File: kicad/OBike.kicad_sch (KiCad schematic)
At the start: 74 parts, among them J1 F34G-1A7Q1-E8C40, J2 Micro_SD_Card_Det1, J3 Conn_01x02, J4 Conn_01x04, J5 U.FL-R-SMT-1_10_, J6 Conn_01x02, J7 Conn_01x05, J8 Conn_01x02, Q1 SS8050, Q2 SS8050, SW1 5_position_tactile, U1 DPS368XTSA1, U10 MAX40200AUK, U2 DS3231M, U3 MCP23017_SO, U4 74HC14, U5 Seeed Studio XIAO SAMD21, U6 MAX40200AUK, U7 LC76G, U8 MAX40200AUK, U9 W25N01GVZEIG_TR

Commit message: purchased PCBs
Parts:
- removed R13: 0R, Resistor_SMD:R_0603_1608Metric, symbol Device:R
- removed U2: DS3231M, Package_SO:SOIC-8_3.9x4.9mm_P1.27mm, symbol Timer_RTC:DS3231M
- added U2: PCF8523T, Package_SO:SOIC-8_3.9x4.9mm_P1.27mm, symbol Timer_RTC:PCF8523T
- C1, C10, C11, C12, C13, C14, C18, C19, C3, C4, C5, C6, C7, C8, C9: MANUFACTURER (none) -> Samsung
- C16, C17, C20, C21: MANUFACTURER (none) -> KEMET
- C2: Digikey PN (none) -> 1276-1066-1-ND; MANUFACTURER 1276-1066-1-ND -> Samsung
- D1, D2, D3, D4, D5: MANUFACTURER (none) -> SMC Diode Solutions
- D6, D7: MANUFACTURER (none) -> STMicroelectronics
- J2: MANUFACTURER (none) -> Same Sky
- J3: MANUFACTURER (none) -> JST
- LS1: value ASI09N40MTRQ -> BUZZER MAGNETIC 5V8.5X8.5 SMD; footprint Mallory:ASI09N40M -> CUI:CUI_CMT-8540S-SMT; Digikey PN 458-ASI09N40MTRQCT-ND -> 102-3746-1-ND; MANUFACTURER (none) -> Same Sky (Formerly CUI Devices)
- Q1, Q2: MANUFACTURER (none) -> MCC
- R36: Digikey PN RMCF0805JT10K0CT-ND -> RMCF0603JT47R0CT-ND
- SW1: MANUFACTURER (none) -> TE Connectivity
- U1: MANUFACTURER (none) -> Infineon Technologies
- U10, U6, U8: MANUFACTURER (none) -> Analog Devices Inc
- U3: MANUFACTURER (none) -> Microchip
- U4: MANUFACTURER (none) -> Toshiba Semiconductor
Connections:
- net 3V3: now also U2.8 (VDD)
- net GND: now also U2.4 (VSS)
- net SCL: now also U2.6 (SCL)
- net SDA: now also U2.5 (SDA)

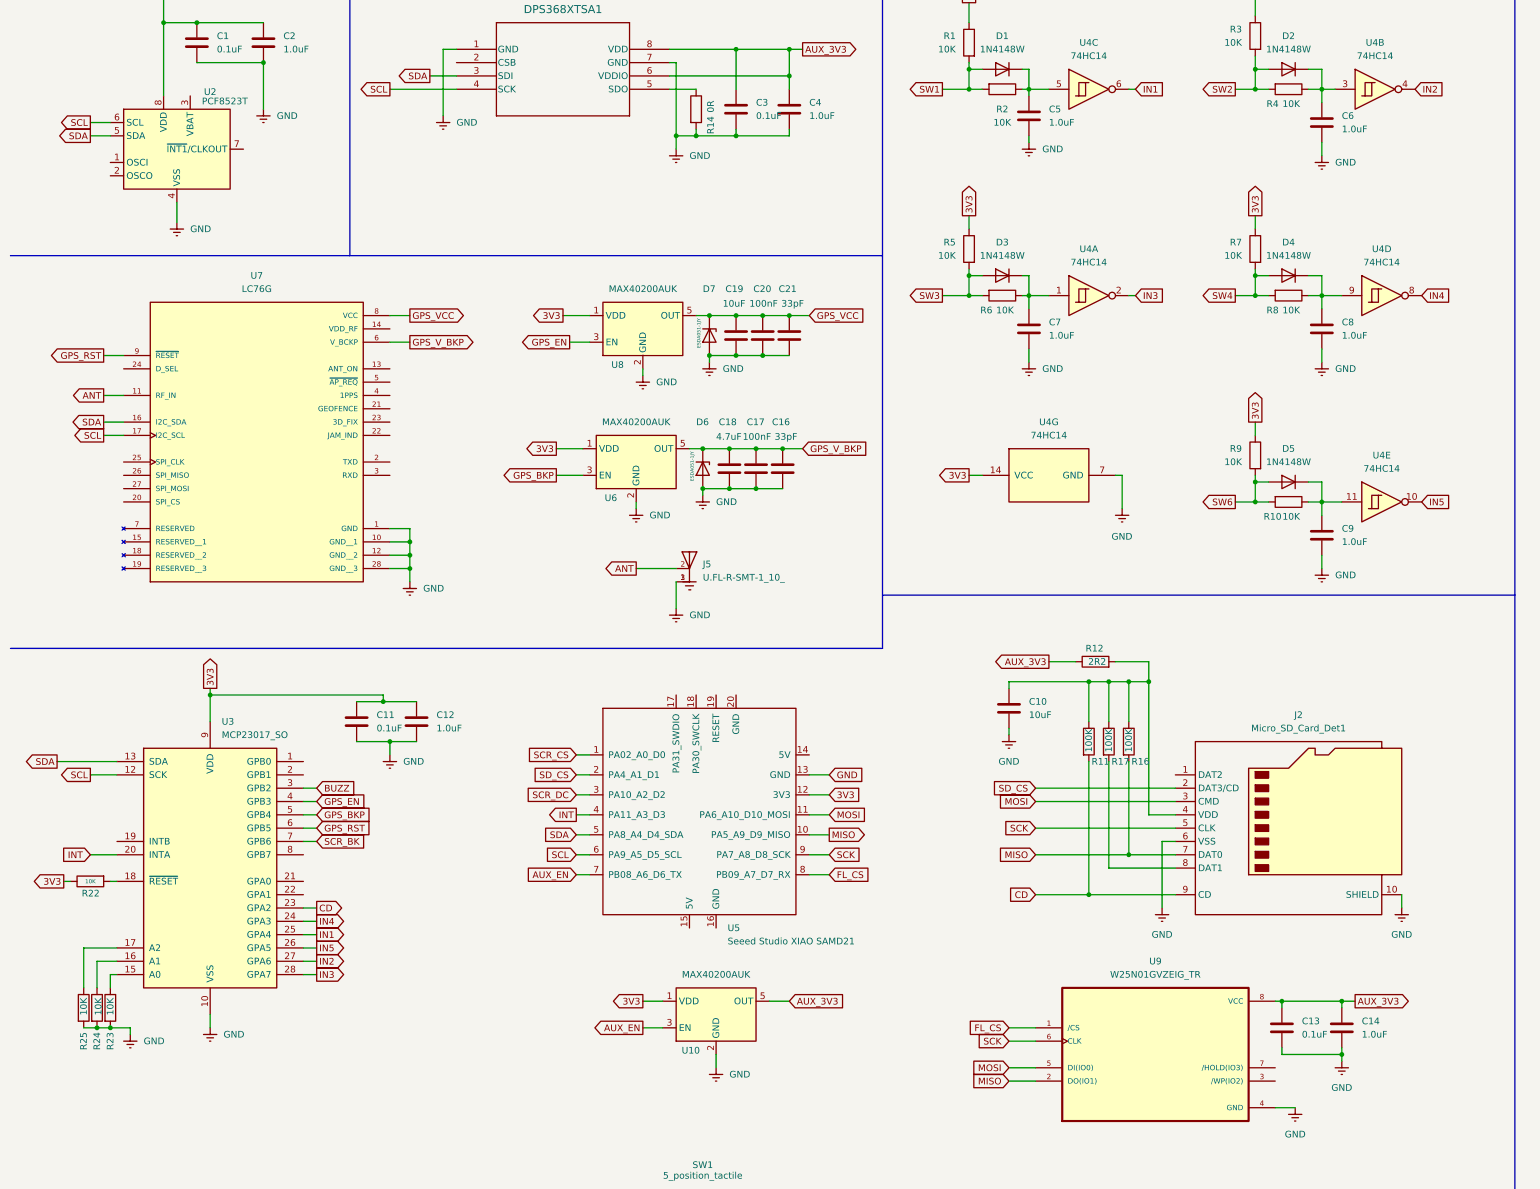
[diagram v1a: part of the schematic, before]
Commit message: pcb fixes
- WP and Hold pins on flash shorted to aux 3v3
- added a 32.768khz crystal for the RTC
- fixed wrong part numbers for Q1 & Q2
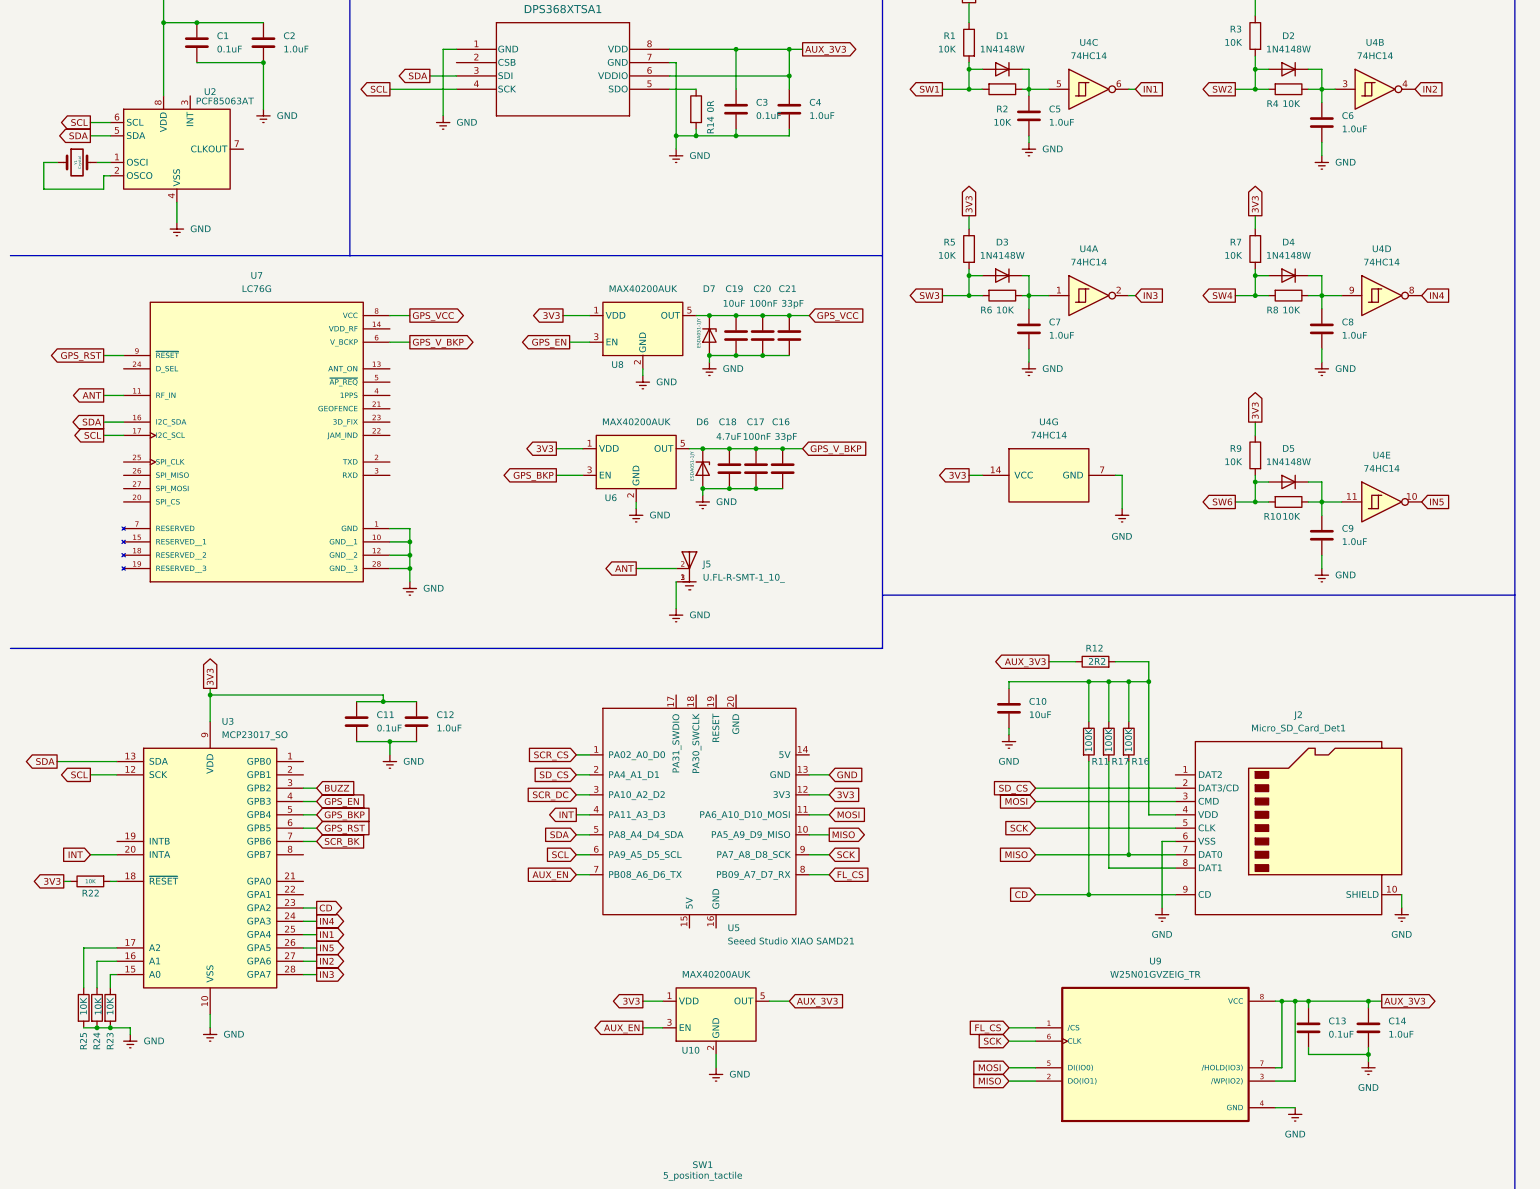
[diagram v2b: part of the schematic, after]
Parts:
- added Y1: Crystal, Jauch:OSCSC320X150X90, symbol Device:Crystal
- Q1, Q2: Digikey PN MMSS8550-H-TPMSCT-ND -> MMSS8050-H-TPMSCT-ND
- U2: value PCF8523T -> PCF85063AT
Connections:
- net AUX_3V3: now also U9.3 (/WP(IO2)), U9.7 (/HOLD(IO3))
- net at U2.1 (OSCI): now also Y1.2
- net at U2.2 (OSCO): now also Y1.1
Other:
- moved on the sheet: C13, C14

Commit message: ui updates
- also disp reset working
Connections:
- net SCR_RST: now reaches J1.15
- net SCR_RST: now also U3.8 (GPB7)
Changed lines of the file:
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@@
 	(wire
 		(pts
+			(xy 364.49 59.69) (xy 382.27 59.69)
+		)
+		(stroke
+			(width 0)
+			(type default)
+		)
+	)
+	(wire
+		(pts
 			(xy 396.24 233.68) (xy 396.24 240.03)
 		)
@@
 	(wire
 		(pts
+			(xy 68.58 185.42) (xy 71.12 185.42)
+		)
+		(stroke
+			(width 0)
+			(type default)
+		)
+	)
+	(wire
+		(pts
 			(xy 29.21 205.74) (xy 29.21 210.82)
 		)
@@
 		)
 	)
+	(global_label "SCR_RST"
+		(shape output)
+		(at 364.49 59.69 180)
+		(fields_autoplaced yes)
+		(effects
+			(font
+				(size 1.27 1.27)
+			)
+			(justify right)
+		)
+		(property "Intersheetrefs" "${INTERSHEET_REFS}"
+			(at 353.3406 59.69 0)
+			(effects
+				(font
+					(size 1.27 1.27)
+				)
+				(justify right)
+				(hide yes)
+			)
+		)
+	)
 	(global_label "AUX_3V3"
 		(shape output)
@@
 				(hide yes)
 			)
+		)
+	)
+	(global_label "SCR_RST"
+		(shape input)
+		(at 71.12 185.42 0)
+		(fields_autoplaced yes)
+		(effects
+			(font
+				(size 1.27 1.27)
+			)
+			(justify left)
+		)
+		(property "Intersheetrefs" "${INTERSHEET_REFS}"
+			(at 82.2694 185.42 0)
+			(effects
+				(font
+					(size 1.27 1.27)
+				)
+				(justify left)
+				(hide yes)
+			)
